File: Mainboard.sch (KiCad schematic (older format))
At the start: 24 parts

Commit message: added usb uart bridge
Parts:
- removed J?: PROGRAM, symbol Connector:Conn_01x04_Female
- added J?: USB_B, symbol Connector:USB_B
- added R?: 22k1, symbol Device:R_Small
- added R?: 47k5, symbol Device:R_Small
- added U?: CP2102N-A01-GQFN24, Package_DFN_QFN:QFN-24-1EP_4x4mm_P0.5mm_EP2.6x2.6mm, symbol Interface_USB:CP2102N-A01-GQFN24
- C? (x2): value 1nf -> 1nF
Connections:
- wire segments 87 -> 99
- no-connect marks 0 -> 11
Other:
- moved on the sheet: C?, D?, J?, R?, SW?

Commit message: updated usb uart bridge
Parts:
- removed D?: PWR_LED, symbol Device:LED
- removed R?: 470, symbol Device:R_Small
- added D?: SP0503BAHT, Package_TO_SOT_SMD:SOT-143, symbol Power_Protection:SP0503BAHT
- added D?: PWR_LED, symbol Device:LED_Small
- added Q? (x2): S8050, Package_TO_SOT_THT:TO-92_Inline, symbol Transistor_BJT:S8050
- added R? (x2): 12k1, symbol Device:R_Small
- added R?: 1k, symbol Device:R_Small
- added R?: 470, symbol Device:R_Small
- C?: value 10uF -> 4.7uF
- C?: value 10uF -> 0.1uF
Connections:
- net labels added: DTR, RTS
- wire segments 99 -> 127
- no-connect marks 11 -> 10
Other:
- moved on the sheet: C?, D?, J?, R?, U?

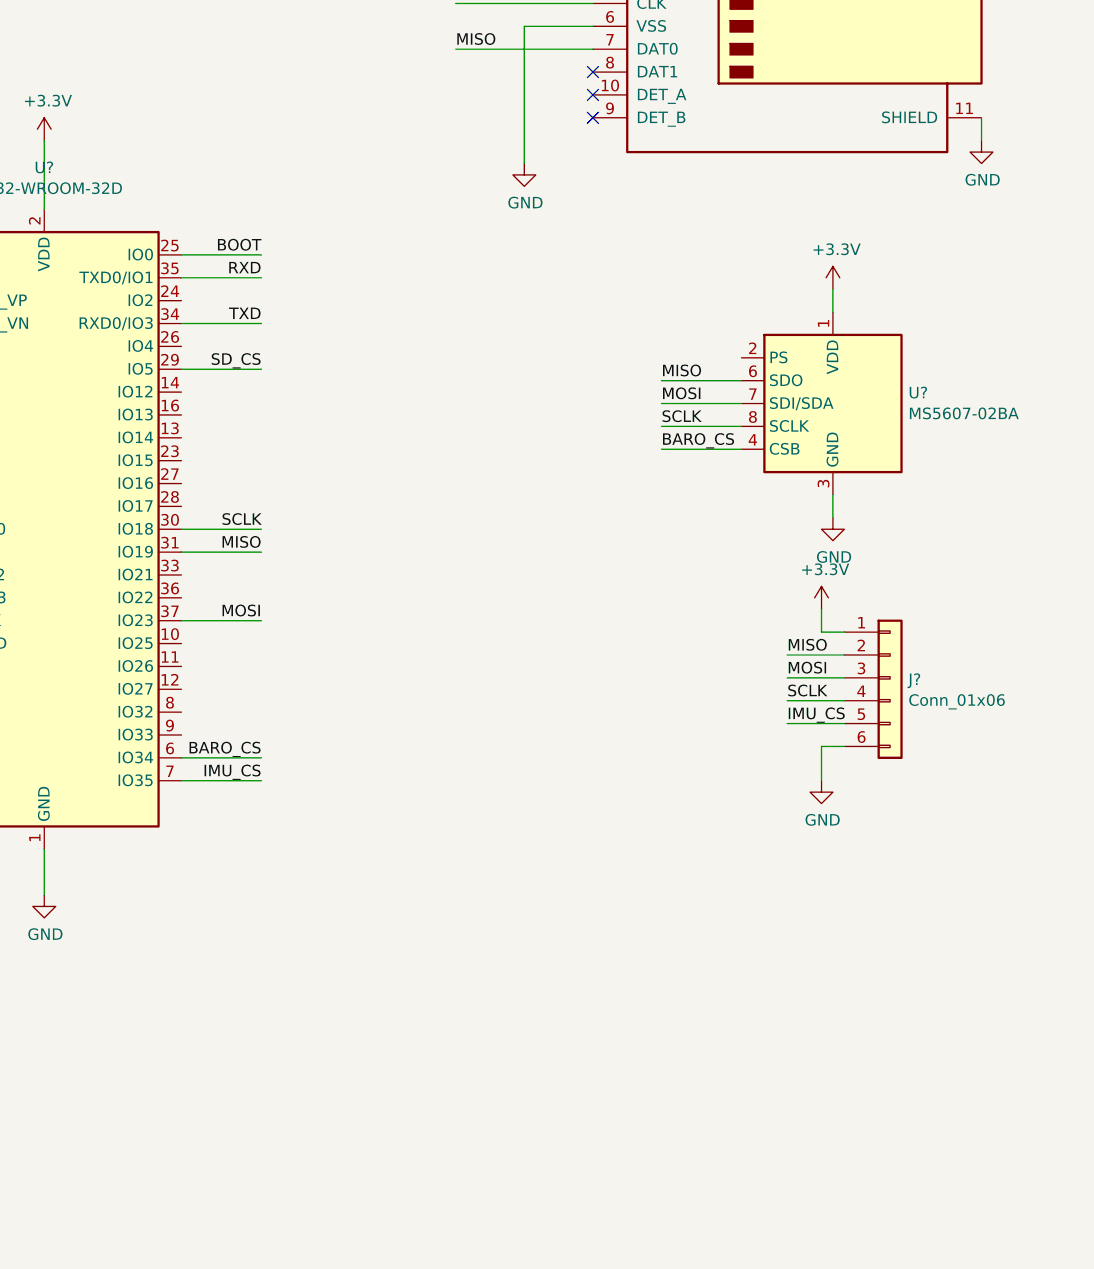
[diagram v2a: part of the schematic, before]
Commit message: added ethernet port for can bus and xbee
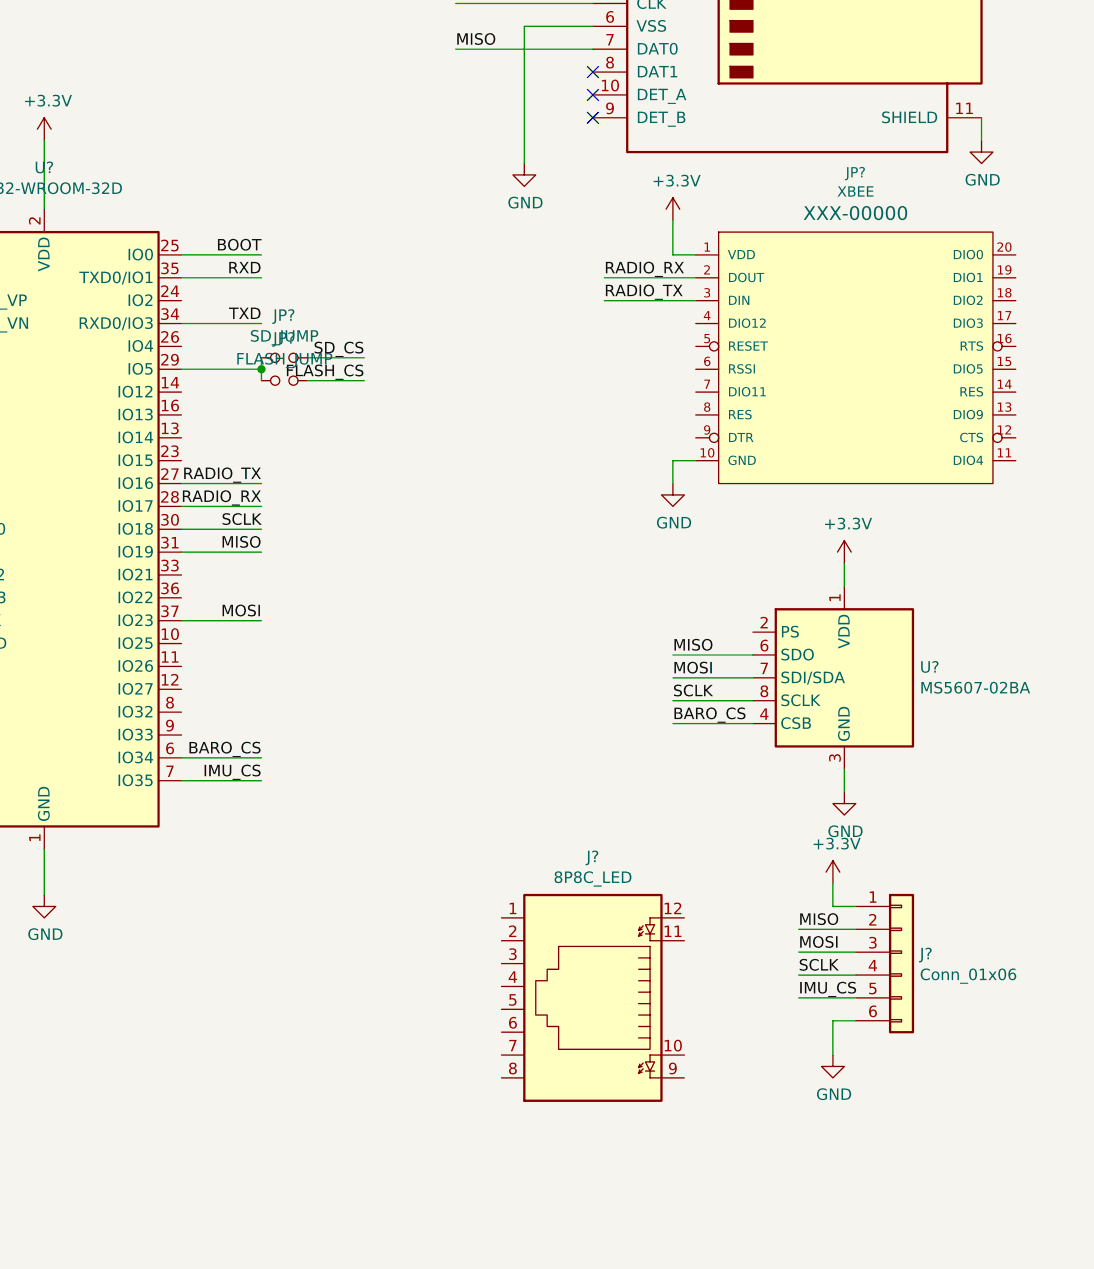
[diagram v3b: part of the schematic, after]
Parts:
- added J?: 8P8C_LED, symbol Connector:8P8C_LED
- added JP?: SD_JUMP, symbol Device:Jumper_NO_Small
- added JP?: FLASH_JUMP, symbol Device:Jumper_NO_Small
- added JP?: XBEE, XBEE, symbol Sparkfun_RF:XBEE
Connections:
- net +3V3: now also JP?.1 (VDD)
- net GND: now also JP?.10 (GND)
- net SD_CS: now also JP?.2; no longer U?.29 (IO5)
- net RADIO_TX: now reaches U?.27 (IO16)
- net RADIO_TX: now also JP?.3 (DIN)
- net RADIO_RX: now reaches U?.28 (IO17)
- net RADIO_RX: now also JP?.2 (DOUT)
- new net: JP?.1, JP?.1, U?.29 (IO5)
- new net FLASH_CS: JP?.2
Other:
- moved on the sheet: J?, U?
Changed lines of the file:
@@
 	8050 1650 8650 1650
-Wire Wire Line
-	8050 1150 8650 1150
-Text Label 8050 1150 0    50   ~ 0
-SD_CS
 Wire Wire Line
 	8350 1350 8650 1350
@@
 Text Label 7200 3750 2    50   ~ 0
 SCLK
-Text Label 7200 3050 2    50   ~ 0
-SD_CS
 Wire Wire Line
 	8050 1250 8650 1250
@@
 Text Label 1100 1100 2    50   ~ 0
 VIN
-$Comp
-L Sensor_Pressure:MS5607-02BA U?
-U 1 1 5DAF7991
-P 9700 3200
-F 0 "U?" H 10030 3246 50  0000 L CNN
-F 1 "MS5607-02BA" H 10030 3155 50  0000 L CNN
-F 2 "Package_LGA:LGA-8_3x5mm_P1.25mm" H 9700 3200 50  0001 C CNN
-F 3 "https://www.te.com/commerce/DocumentDelivery/DDEController?Action=showdoc&DocId=Data+Sheet%7FMS5607-02BA03%7FB2%7Fpdf%7FEnglish%7FENG_DS_MS5607-02BA03_B2.pdf%7FCAT-BLPS0035" H 9700 3200 50  0001 C CNN
-	1    9700 3200
-	1    0    0    -1
-$EndComp
-$Comp
-L power:+3.3V #PWR?
-U 1 1 5DAF89F9
-P 9700 2700
-F 0 "#PWR?" H 9700 2550 50  0001 C CNN
-F 1 "+3.3V" H 9715 2873 50  0000 C CNN
-F 2 "" H 9700 2700 50  0001 C CNN
-F 3 "" H 9700 2700 50  0001 C CNN
-	1    9700 2700
-	1    0    0    -1
-$EndComp
-Wire Wire Line
-	9700 2700 9700 2800
-$Comp
-L power:GND #PWR?
-U 1 1 5DAFAAA1
-P 9700 3700
-F 0 "#PWR?" H 9700 3450 50  0001 C CNN
-F 1 "GND" H 9705 3527 50  0000 C CNN
-F 2 "" H 9700 3700 50  0001 C CNN
-F 3 "" H 9700 3700 50  0001 C CNN
-	1    9700 3700
-	1    0    0    -1
-$EndComp
-Wire Wire Line
-	9700 3700 9700 3600
-Text Label 8950 3100 0    50   ~ 0
-MISO
-Text Label 8950 3200 0    50   ~ 0
-MOSI
-Text Label 8950 3300 0    50   ~ 0
-SCLK
-Text Label 8950 3400 0    50   ~ 0
-BARO_CS
-Wire Wire Line
-	8950 3100 9300 3100
-Wire Wire Line
-	8950 3200 9300 3200
-Wire Wire Line
-	8950 3300 9300 3300
-Wire Wire Line
-	8950 3400 9300 3400
 Text Label 7200 4750 2    50   ~ 0
 BARO_CS
@@
 	7200 4850 6850 4850
 Text Label 7200 4850 2    50   ~ 0
-IMU_CS
-$Comp
-L Connector_Generic:Conn_01x06 J?
-U 1 1 5DB7D398
-P 9950 4400
-F 0 "J?" H 10030 4392 50  0000 L CNN
-F 1 "Conn_01x06" H 10030 4301 50  0000 L CNN
-F 2 "" H 9950 4400 50  0001 C CNN
-F 3 "~" H 9950 4400 50  0001 C CNN
-	1    9950 4400
-	1    0    0    -1
-$EndComp
-$Comp
-L power:+3.3V #PWR?
-U 1 1 5DB7DB84
-P 9650 4100
-F 0 "#PWR?" H 9650 3950 50  0001 C CNN
-F 1 "+3.3V" H 9665 4273 50  0000 C CNN
-F 2 "" H 9650 4100 50  0001 C CNN
-F 3 "" H 9650 4100 50  0001 C CNN
-	1    9650 4100
-	1    0    0    -1
-$EndComp
-Wire Wire Line
-	9650 4100 9650 4200
-Wire Wire Line
-	9650 4200 9750 4200
-$Comp
-L power:GND #PWR?
-U 1 1 5DB803B2
-P 9650 4850
-F 0 "#PWR?" H 9650 4600 50  0001 C CNN
-F 1 "GND" H 9655 4677 50  0000 C CNN
-F 2 "" H 9650 4850 50  0001 C CNN
-F 3 "" H 9650 4850 50  0001 C CNN
-	1    9650 4850
-	1    0    0    -1
-$EndComp
-Wire Wire Line
-	9650 4850 9650 4700
-Wire Wire Line
-	9650 4700 9750 4700
-Wire Wire Line
-	9500 4300 9750 4300
-Wire Wire Line
-	9500 4400 9750 4400
-Wire Wire Line
-	9500 4500 9750 4500
-Wire Wire Line
-	9500 4600 9750 4600
-Text Label 9500 4300 0    50   ~ 0
-MISO
-Text Label 9500 4400 0    50   ~ 0
-MOSI
-Text Label 9500 4500 0    50   ~ 0
-SCLK
-Text Label 9500 4600 0    50   ~ 0
 IMU_CS
 $Comp
@@
 	1050 3050 1250 3050
 Connection ~ 1050 4000
+$Comp
+L Device:Jumper_NO_Small JP?
+U 1 1 5DAF9D41
+P 7300 3000
+F 0 "JP?" H 7300 3185 50  0000 C CNN
+F 1 "SD_JUMP" H 7300 3094 50  0000 C CNN
+F 2 "" H 7300 3000 50  0001 C CNN
+F 3 "~" H 7300 3000 50  0001 C CNN
+	1    7300 3000
+	1    0    0    -1
+$EndComp
+Text Label 8050 1150 0    50   ~ 0
+SD_CS
+Wire Wire Line
+	8050 1150 8650 1150
+$Comp
+L Device:Jumper_NO_Small JP?
+U 1 1 5DB2151C
+P 7300 3100
+F 0 "JP?" H 7300 3285 50  0000 C CNN
+F 1 "FLASH_JUMP" H 7300 3194 50  0000 C CNN
+F 2 "" H 7300 3100 50  0001 C CNN
+F 3 "~" H 7300 3100 50  0001 C CNN
+	1    7300 3100
+	1    0    0    -1
+$EndComp
+Wire Wire Line
+	7200 3100 7200 3050
+Connection ~ 7200 3050
+Wire Wire Line
+	7200 3050 7200 3000
+Wire Wire Line
+	7400 3000 7650 3000
+Wire Wire Line
+	7400 3100 7650 3100
+Text Label 7650 3000 2    50   ~ 0
+SD_CS
+Text Label 7650 3100 2    50   ~ 0
+FLASH_CS
+$Comp
+L Sensor_Pressure:MS5607-02BA U?
+U 1 1 5DAF7991
+P 9750 4400
+F 0 "U?" H 10080 4446 50  0000 L CNN
+F 1 "MS5607-02BA" H 10080 4355 50  0000 L CNN
+F 2 "Package_LGA:LGA-8_3x5mm_P1.25mm" H 9750 4400 50  0001 C CNN
+F 3 "https://www.te.com/commerce/DocumentDelivery/DDEController?Action=showdoc&DocId=Data+Sheet%7FMS5607-02BA03%7FB2%7Fpdf%7FEnglish%7FENG_DS_MS5607-02BA03_B2.pdf%7FCAT-BLPS0035" H 9750 4400 50  0001 C CNN
+	1    9750 4400
+	1    0    0    -1
+$EndComp
+$Comp
+L power:+3.3V #PWR?
+U 1 1 5DAF89F9
+P 9750 3900
+F 0 "#PWR?" H 9750 3750 50  0001 C CNN
+F 1 "+3.3V" H 9765 4073 50  0000 C CNN
+F 2 "" H 9750 3900 50  0001 C CNN
+F 3 "" H 9750 3900 50  0001 C CNN
+	1    9750 3900
+	1    0    0    -1
+$EndComp
+Wire Wire Line
+	9750 3900 9750 4000
+$Comp
+L power:GND #PWR?
+U 1 1 5DAFAAA1
+P 9750 4900
+F 0 "#PWR?" H 9750 4650 50  0001 C CNN
+F 1 "GND" H 9755 4727 50  0000 C CNN
+F 2 "" H 9750 4900 50  0001 C CNN
+F 3 "" H 9750 4900 50  0001 C CNN
+	1    9750 4900
+	1    0    0    -1
+$EndComp
+Wire Wire Line
+	9750 4900 9750 4800
+Text Label 9000 4300 0    50   ~ 0
+MISO
+Text Label 9000 4400 0    50   ~ 0
+MOSI
+Text Label 9000 4500 0    50   ~ 0
+SCLK
+Text Label 9000 4600 0    50   ~ 0
+BARO_CS
+Wire Wire Line
+	9000 4300 9350 4300
+Wire Wire Line
+	9000 4400 9350 4400
+Wire Wire Line
+	9000 4500 9350 4500
+Wire Wire Line
+	9000 4600 9350 4600
+$Comp
+L Connector_Generic:Conn_01x06 J?
+U 1 1 5DB7D398
+P 10000 5600
+F 0 "J?" H 10080 5592 50  0000 L CNN
+F 1 "Conn_01x06" H 10080 5501 50  0000 L CNN
+F 2 "" H 10000 5600 50  0001 C CNN
+F 3 "~" H 10000 5600 50  0001 C CNN
+	1    10000 5600
+	1    0    0    -1
+$EndComp
+$Comp
+L power:+3.3V #PWR?
+U 1 1 5DB7DB84
+P 9700 5300
+F 0 "#PWR?" H 9700 5150 50  0001 C CNN
+F 1 "+3.3V" H 9715 5473 50  0000 C CNN
+F 2 "" H 9700 5300 50  0001 C CNN
+F 3 "" H 9700 5300 50  0001 C CNN
+	1    9700 5300
+	1    0    0    -1
+$EndComp
+Wire Wire Line
+	9700 5300 9700 5400
+Wire Wire Line
+	9700 5400 9800 5400
+$Comp
+L power:GND #PWR?
+U 1 1 5DB803B2
+P 9700 6050
+F 0 "#PWR?" H 9700 5800 50  0001 C CNN
+F 1 "GND" H 9705 5877 50  0000 C CNN
+F 2 "" H 9700 6050 50  0001 C CNN
+F 3 "" H 9700 6050 50  0001 C CNN
+	1    9700 6050
+	1    0    0    -1
+$EndComp
+Wire Wire Line
+	9700 6050 9700 5900
+Wire Wire Line
+	9700 5900 9800 5900
+Wire Wire Line
+	9550 5500 9800 5500
+Wire Wire Line
+	9550 5600 9800 5600
+Wire Wire Line
+	9550 5700 9800 5700
+Wire Wire Line
+	9550 5800 9800 5800
+Text Label 9550 5500 0    50   ~ 0
+MISO
+Text Label 9550 5600 0    50   ~ 0
+MOSI
+Text Label 9550 5700 0    50   ~ 0
+SCLK
+Text Label 9550 5800 0    50   ~ 0
+IMU_CS
+Wire Wire Line
+	6850 3550 7200 3550
+Wire Wire Line
+	6850 3650 7200 3650
+Text Label 7200 3650 2    50   ~ 0
+RADIO_RX
+Text Label 7200 3550 2    50   ~ 0
+RADIO_TX
+$Comp
+L Sparkfun_RF:XBEE JP?
+U 1 1 5DB6F306
+P 9800 2950
+F 0 "JP?" H 9800 3710 45  0000 C CNN
+F 1 "XBEE" H 9800 3626 45  0000 C CNN
+F 2 "XBEE" H 9800 3550 20  0001 C CNN
+F 3 "" H 9800 2950 50  0001 C CNN
+F 4 "XXX-00000" H 9800 3531 60  0000 C CNN "Field4"
+	1    9800 2950
+	1    0    0    -1
+$EndComp
+$Comp
+L power:GND #PWR?
+U 1 1 5DB72471
+P 9000 3550
+F 0 "#PWR?" H 9000 3300 50  0001 C CNN
+F 1 "GND" H 9005 3377 50  0000 C CNN
+F 2 "" H 9000 3550 50  0001 C CNN
+F 3 "" H 9000 3550 50  0001 C CNN
+	1    9000 3550
+	1    0    0    -1
+$EndComp
+Wire Wire Line
+	9100 3450 9000 3450
+Wire Wire Line
+	9000 3450 9000 3550
+$Comp
+L power:+3.3V #PWR?
+U 1 1 5DB78938
+P 9000 2400
+F 0 "#PWR?" H 9000 2250 50  0001 C CNN
+F 1 "+3.3V" H 9015 2573 50  0000 C CNN
+F 2 "" H 9000 2400 50  0001 C CNN
+F 3 "" H 9000 2400 50  0001 C CNN
+	1    9000 2400
+	1    0    0    -1
+$EndComp
+Wire Wire Line
+	9000 2400 9000 2550
+Wire Wire Line
+	9000 2550 9100 2550
+Wire Wire Line
+	9100 2750 8700 2750
+Wire Wire Line
+	9100 2650 8700 2650
+Text Label 8700 2650 0    50   ~ 0
+RADIO_RX
+Text Label 8700 2750 0    50   ~ 0
+RADIO_TX
+$Comp
+L Connector:8P8C_LED J?
+U 1 1 5DB9241E
+P 8650 5750
+F 0 "J?" H 8650 5183 50  0000 C CNN
+F 1 "8P8C_LED" H 8650 5274 50  0000 C CNN
+F 2 "" V 8650 5775 50  0001 C CNN
+F 3 "~" V 8650 5775 50  0001 C CNN
+	1    8650 5750
+	-1   0    0    1
+$EndComp
 $EndSCHEMATC

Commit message: update
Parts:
- added U?: MCP2515-xSO, Package_SO:SOIC-18W_7.5x11.6mm_P1.27mm, symbol Interface_CAN_LIN:MCP2515-xSO
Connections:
- net CAN_HIGH: now reaches J?.1
- net CAN_LOW: now reaches J?.2
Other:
- moved on the sheet: C?, R?, SW?

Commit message: added gps
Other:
- moved on the sheet: J?, JP?, U?

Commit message: update
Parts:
- removed JP?: SD_JUMP, symbol Device:Jumper_NO_Small
- removed JP?: FLASH_JUMP, symbol Device:Jumper_NO_Small
- added JP?: SolderJumper_3_Open, symbol Jumper:SolderJumper_3_Open
- added R? (x2): 4.7K, symbol Device:R_Small
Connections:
- net labels added: SCL, SDA
- net labels removed: sda
- wire segments 141 -> 148
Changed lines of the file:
@@
 $Descr A4 11693 8268
 encoding utf-8
-Sheet 1 1
+Sheet 1 2
 Title ""
 Date ""
@@
 Comment4 ""
 $EndDescr
-$Comp
-L RF_Module:ESP32-WROOM-32D U?
-U 1 1 5DA5F4C7
-P 6250 3750
-F 0 "U?" H 6250 5331 50  0000 C CNN
-F 1 "ESP32-WROOM-32D" H 6250 5240 50  0000 C CNN
-F 2 "RF_Module:ESP32-WROOM-32" H 6250 2250 50  0001 C CNN
-F 3 "https://www.espressif.com/sites/default/files/documentation/esp32-wroom-32d_esp32-wroom-32u_datasheet_en.pdf" H 5950 3800 50  0001 C CNN
-	1    6250 3750
-	1    0    0    -1
-$EndComp
 $Comp
 L power:+3.3V #PWR?
@@
 	1050 3050 1250 3050
 Connection ~ 1050 4000
-$Comp
-L Device:Jumper_NO_Small JP?
-U 1 1 5DAF9D41
-P 7300 3000
-F 0 "JP?" H 7300 3185 50  0000 C CNN
-F 1 "SD_JUMP" H 7300 3094 50  0000 C CNN
-F 2 "" H 7300 3000 50  0001 C CNN
-F 3 "~" H 7300 3000 50  0001 C CNN
-	1    7300 3000
-	1    0    0    -1
-$EndComp
 Text Label 8700 1150 0    50   ~ 0
 SD_CS
 Wire Wire Line
 	8700 1150 9300 1150
-$Comp
-L Device:Jumper_NO_Small JP?
-U 1 1 5DB2151C
-P 7300 3100
-F 0 "JP?" H 7300 3285 50  0000 C CNN
-F 1 "FLASH_JUMP" H 7300 3194 50  0000 C CNN
-F 2 "" H 7300 3100 50  0001 C CNN
-F 3 "~" H 7300 3100 50  0001 C CNN
-	1    7300 3100
-	1    0    0    -1
-$EndComp
-Wire Wire Line
-	7200 3100 7200 3050
-Connection ~ 7200 3050
-Wire Wire Line
-	7200 3050 7200 3000
-Wire Wire Line
-	7400 3000 7650 3000
-Wire Wire Line
-	7400 3100 7650 3100
-Text Label 7650 3000 2    50   ~ 0
+Wire Wire Line
+	7350 2850 7600 2850
+Wire Wire Line
+	7350 3250 7600 3250
+Text Label 7600 2850 2    50   ~ 0
 SD_CS
-Text Label 7650 3100 2    50   ~ 0
+Text Label 7600 3250 2    50   ~ 0
 FLASH_CS
 $Comp
@@
 Text Label 7900 5550 0    50   ~ 0
 CAN_LOW
+$Comp
+L RF_Module:ESP32-WROOM-32D U?
+U 1 1 5DA5F4C7
+P 6250 3750
+F 0 "U?" H 6250 5331 50  0000 C CNN
+F 1 "ESP32-WROOM-32D" H 6250 5240 50  0000 C CNN
+F 2 "RF_Module:ESP32-WROOM-32" H 6250 2250 50  0001 C CNN
+F 3 "https://www.espressif.com/sites/default/files/documentation/esp32-wroom-32d_esp32-wroom-32u_datasheet_en.pdf" H 5950 3800 50  0001 C CNN
+	1    6250 3750
+	1    0    0    -1
+$EndComp
+Text Label 7600 3950 2    50   ~ 0
+SDA
+Text Label 7600 4050 2    50   ~ 0
+SCL
+$Comp
+L Jumper:SolderJumper_3_Open JP?
+U 1 1 5DC01BB6
+P 7350 3050
+F 0 "JP?" V 7304 3118 50  0000 L CNN
+F 1 "SolderJumper_3_Open" V 7395 3118 50  0000 L CNN
+F 2 "" H 7350 3050 50  0001 C CNN
+F 3 "~" H 7350 3050 50  0001 C CNN
+	1    7350 3050
+	0    1    1    0
+$EndComp
+Wire Wire Line
+	6850 3950 7300 3950
+Wire Wire Line
+	6850 4050 7400 4050
+Wire Wire Line
+	7400 4050 7400 3850
+Connection ~ 7400 4050
+Wire Wire Line
+	7400 4050 7600 4050
+Wire Wire Line
+	7300 3950 7300 3850
+Connection ~ 7300 3950
+Wire Wire Line
+	7300 3950 7600 3950
+$Comp
+L Device:R_Small R?
+U 1 1 5DB1BC5B
+P 7400 3750
+F 0 "R?" H 7459 3796 50  0000 L CNN
+F 1 "4.7K" H 7459 3705 50  0000 L CNN
+F 2 "" H 7400 3750 50  0001 C CNN
+F 3 "~" H 7400 3750 50  0001 C CNN
+	1    7400 3750
+	1    0    0    -1
+$EndComp
+$Comp
+L Device:R_Small R?
+U 1 1 5DB1C9E2
+P 7300 3750
+F 0 "R?" H 7359 3796 50  0000 L CNN
+F 1 "4.7K" H 7359 3705 50  0000 L CNN
+F 2 "" H 7300 3750 50  0001 C CNN
+F 3 "~" H 7300 3750 50  0001 C CNN
+	1    7300 3750
+	1    0    0    -1
+$EndComp
+Wire Wire Line
+	7300 3650 7350 3650
+$Comp
+L power:+3.3V #PWR?
+U 1 1 5DB29AD6
+P 7350 3600
+F 0 "#PWR?" H 7350 3450 50  0001 C CNN
+F 1 "+3.3V" H 7365 3773 50  0000 C CNN
+F 2 "" H 7350 3600 50  0001 C CNN
+F 3 "" H 7350 3600 50  0001 C CNN
+	1    7350 3600
+	1    0    0    -1
+$EndComp
+Wire Wire Line
+	7350 3600 7350 3650
+Connection ~ 7350 3650
+Wire Wire Line
+	7350 3650 7400 3650
 $Sheet
 S 8400 3050 500  200
@@
 F1 "gps.sch" 50
 $EndSheet
-Text HLabel 8400 3100 0    50   Input ~ 0
-sda
 $EndSCHEMATC
